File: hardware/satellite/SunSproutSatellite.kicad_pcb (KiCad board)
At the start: 4 copper layers, 27.2 x 51.1 mm, 43 parts, among them J1 RJHSE5380_QwiicBusCompatible, J2 Conn_01x03, J3 Conn_01x03, J4 Conn_01x03, J5 Conn_01x03, J6 Conn_01x03, J7 Conn_01x04, J8 Qwiic, J9 Conn_01x04, U1 PCA9615DPZ, U2 ADS1115IDGS, U3 DS2482S-100+, U4 USBLC6-4SC6

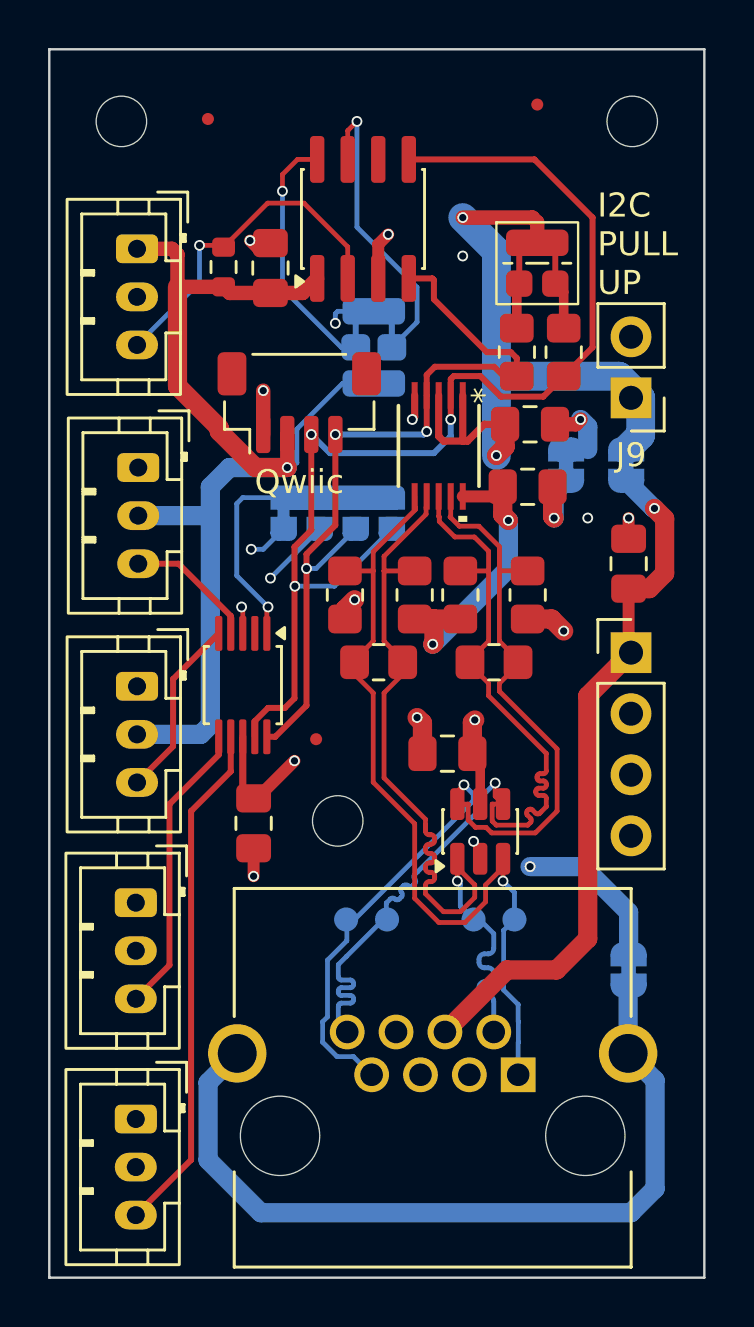
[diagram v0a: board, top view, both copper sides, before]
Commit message: feat(satellite): add power status LED1 and cuttable disconnect jumper JP19
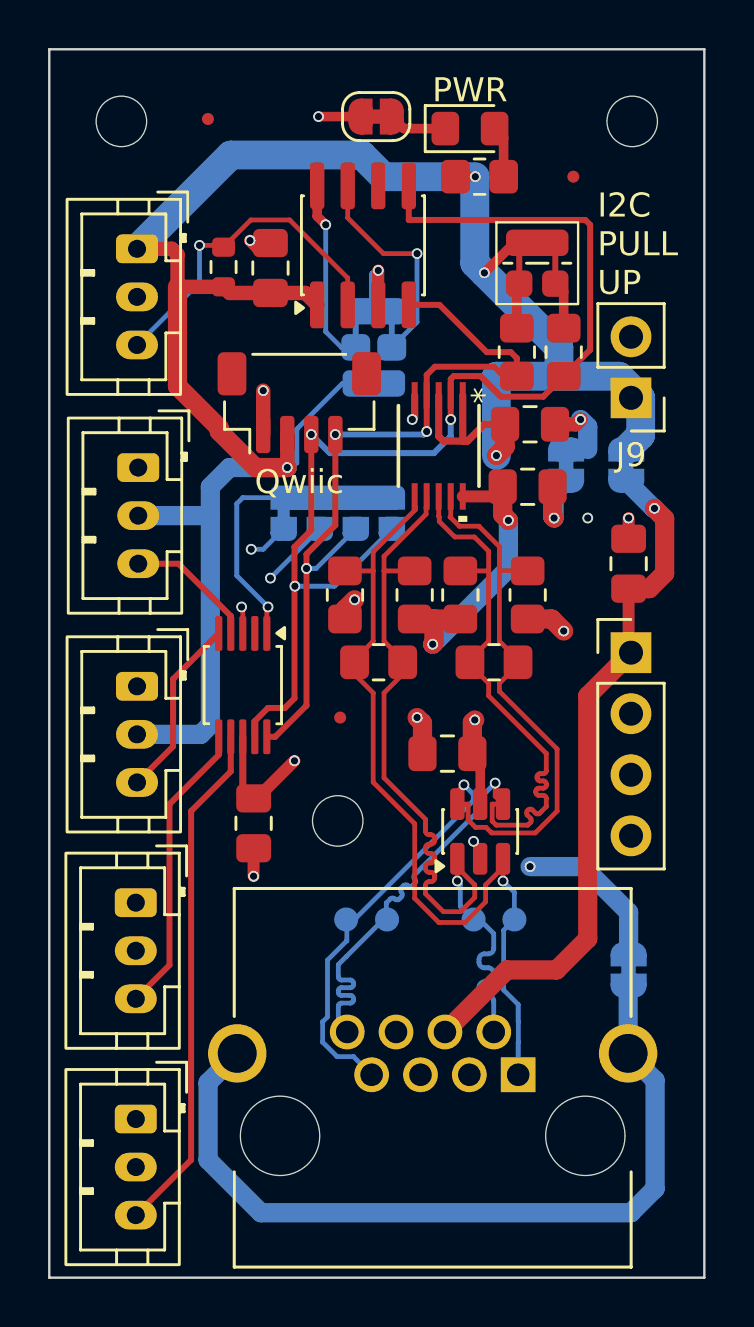
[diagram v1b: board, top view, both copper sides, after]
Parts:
- added JP19: SolderJumper_2_Bridged, Jumper:SolderJumper-2_P1.3mm_Bridged_RoundedPad1.0x1.5mm, F.Cu at (113.6, 102.8)
- added LED1: PWR, LED_SMD:LED_0805_2012Metric_Pad1.15x1.40mm_HandSolder, F.Cu at (117.5, 103.3)
- added R10: 120Ω, Resistor_SMD:R_0805_2012Metric_Pad1.20x1.40mm_HandSolder, F.Cu at (117.9, 105.3)
- moved Ref** 3.35 mm to (121.8, 105.3)
- moved Ref** 1.35 mm to (112.1, 127.8)
- moved U3 1.10 mm to (113.0, 108.2)
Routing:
- net AD0_SEL: track 12.6 -> 9.17 mm
- net AD1_SEL: track 10.5 -> 7.73 mm
- net Net-(JP19-A): track 0.00 -> 2.43 mm
- net /Differential I2C Endpoint/LED1_REGULATED_SOURCE: track 0.00 -> 2.40 mm
- net SCL_LOCAL: track 34.5 -> 33.5 mm
- net GND: track 14.6 -> 15.5 mm, vias 10 -> 9
- net SAT_3V3: track 147.3 -> 148.2 mm, vias 5 -> 6

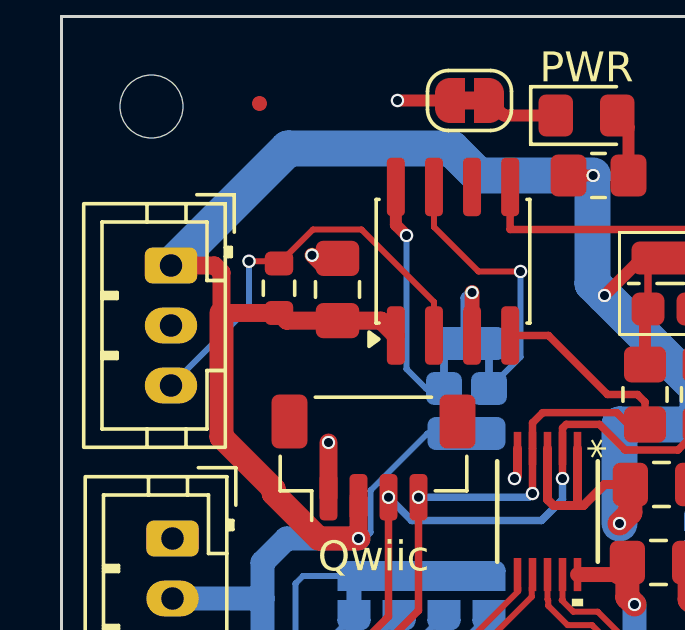
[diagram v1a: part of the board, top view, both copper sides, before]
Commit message: Fixed missed 603 component that was marked DNP
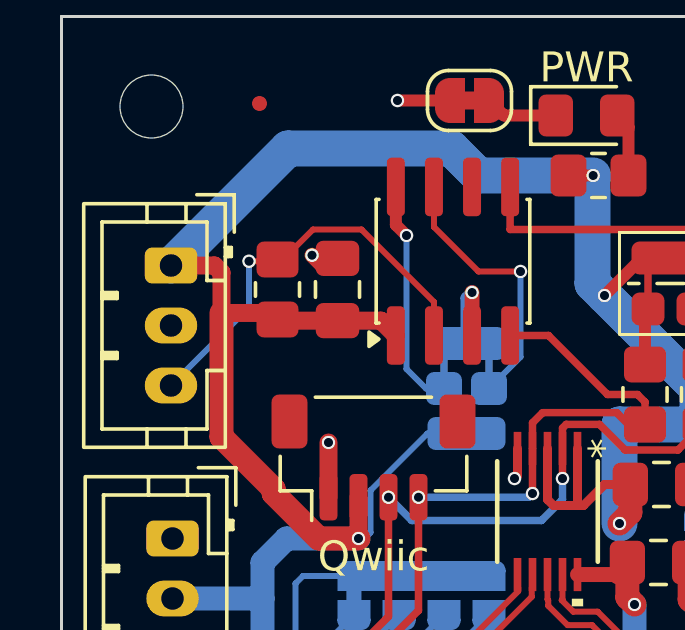
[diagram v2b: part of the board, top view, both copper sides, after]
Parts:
- R9: footprint Resistor_SMD:R_0603_1608Metric -> Resistor_SMD:R_0805_2012Metric_Pad1.20x1.40mm_HandSolder
- moved R9 0.07 mm to (107.2, 109.1)
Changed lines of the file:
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@@
 		(embedded_fonts no)
 	)
-	(footprint "Resistor_SMD:R_0603_1608Metric"
+	(footprint "Resistor_SMD:R_0805_2012Metric_Pad1.20x1.40mm_HandSolder"
 		(layer "F.Cu")
-		(at 107.25 109.0575 90)
-		(descr "Resistor SMD 0603 (1608 Metric), square (rectangular) end terminal, IPC-7351 nominal, (Body size source: IPC-SM-782 page 72, https://www.pcb-3d.com/wordpress/wp-content/uploads/ipc-sm-782a_amendment_1_and_2.pdf)")
-		(tags "resistor")
+		(at 107.2 109.1 90)
+		(descr "Resistor SMD 0805 (2012 Metric), square (rectangular) end terminal, IPC-7351 nominal with elongated pad for handsoldering. (Body size source: IPC-SM-782 page 72, https://www.pcb-3d.com/wordpress/wp-content/uploads/ipc-sm-782a_amendment_1_and_2.pdf)")
+		(tags "resistor handsolder")
 		(property "Reference" "R9"
-			(at 0 -1.43 90)
+			(at 0 -1.65 90)
 			(layer "F.SilkS")
 			(hide yes)
@@
 		)
 		(property "Value" "4.7k"
-			(at 0 1.43 90)
+			(at 0 1.65 90)
 			(layer "F.Fab")
 			(effects
 				(font
-					(size 0.5 0.5)
+					(size 1 1)
+					(thickness 0.15)
 				)
 			)
@@
 			(effects
 				(font
-					(size 1 1)
-					(thickness 0.15)
+					(size 0.5 0.5)
+					(thickness 0.05)
 				)
 			)
@@
 			(effects
 				(font
-					(size 1 1)
-					(thickness 0.15)
+					(size 0.5 0.5)
+					(thickness 0.05)
 				)
 			)
@@
 			(effects
 				(font
-					(size 1 1)
-					(thickness 0.15)
+					(size 0.5 0.5)
+					(thickness 0.05)
 				)
 			)
@@
 			(effects
 				(font
-					(size 1 1)
-					(thickness 0.15)
+					(size 0.5 0.5)
+					(thickness 0.05)
 				)
 			)
@@
 		(duplicate_pad_numbers_are_jumpers no)
 		(fp_line
-			(start -0.237258 -0.5225)
-			(end 0.237258 -0.5225)
+			(start -0.227064 -0.735)
+			(end 0.227064 -0.735)
 			(stroke
 				(width 0.12)
@@
 		)
 		(fp_line
-			(start -0.237258 0.5225)
-			(end 0.237258 0.5225)
+			(start -0.227064 0.735)
+			(end 0.227064 0.735)
 			(stroke
 				(width 0.12)
@@
 		)
 		(fp_rect
-			(start -1.48 -0.73)
-			(end 1.48 0.73)
+			(start -1.85 -0.95)
+			(end 1.85 0.95)
 			(stroke
 				(width 0.05)
@@
 		)
 		(fp_rect
-			(start -0.8 -0.4125)
-			(end 0.8 0.4125)
+			(start -1 -0.625)
+			(end 1 0.625)
 			(stroke
 				(width 0.1)
@@
 				(font
 					(size 0.5 0.5)
+					(thickness 0.08)
 				)
 			)
 		)
 		(pad "1" smd roundrect
-			(at -0.825 0 90)
-			(size 0.8 0.95)
+			(at -1 0 90)
+			(size 1.2 1.4)
 			(layers "F.Cu" "F.Mask" "F.Paste")
-			(roundrect_rratio 0.25)
+			(roundrect_rratio 0.208333)
 			(net "SAT_3V3")
 			(pintype "passive")
 		)
 		(pad "2" smd roundrect
-			(at 0.825 0 90)
-			(size 0.8 0.95)
+			(at 1 0 90)
+			(size 1.2 1.4)
 			(layers "F.Cu" "F.Mask" "F.Paste")
-			(roundrect_rratio 0.25)
+			(roundrect_rratio 0.208333)
 			(net "ONEWIRE_DQ")
 			(pintype "passive")
 		)
 		(embedded_fonts no)
-		(model "kicad-embed://R_0603_1608Metric.step"
+		(model "${KICAD10_3DMODEL_DIR}/Resistor_SMD.3dshapes/R_0805_2012Metric.step"
 			(offset
 				(xyz 0 0 0)
@@
 	)
 	(segment
-		(start 108.3825 107.1)
-		(end 110 107.1)
+		(start 107.325 108.1575)
+		(end 108.3825 107.1)
 		(width 0.2)
 		(layer "F.Cu")
@@
 	)
 	(segment
-		(start 106.25 108.1575)
-		(end 107.325 108.1575)
+		(start 110 107.1)
+		(end 112.415 109.515)
 		(width 0.2)
 		(layer "F.Cu")
@@
 	)
 	(segment
-		(start 107.325 108.1575)
-		(end 108.3825 107.1)
+		(start 108.3825 107.1)
+		(end 110 107.1)
 		(width 0.2)
 		(layer "F.Cu")
@@
 	)
 	(segment
-		(start 110 107.1)
-		(end 112.415 109.515)
+		(start 106.25 108.1575)
+		(end 107.325 108.1575)
 		(width 0.2)
 		(layer "F.Cu")
@@
 	(segment
 		(start 106.25 109.7)
-		(end 106.25 108.1575)
+		(end 103.65 112.3)
 		(width 0.2)
 		(layer "B.Cu")
@@
 	)
 	(segment
-		(start 103.65 112.3)
+		(start 106.25 108.1575)
 		(end 106.25 109.7)
 		(width 0.2)
